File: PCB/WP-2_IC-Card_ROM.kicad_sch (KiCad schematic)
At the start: 9 parts, among them J1 SMS-138-01-G-S, SW1 CUS-12TB, SW2 CUS-12TB, U1 29F0x0_TSOP

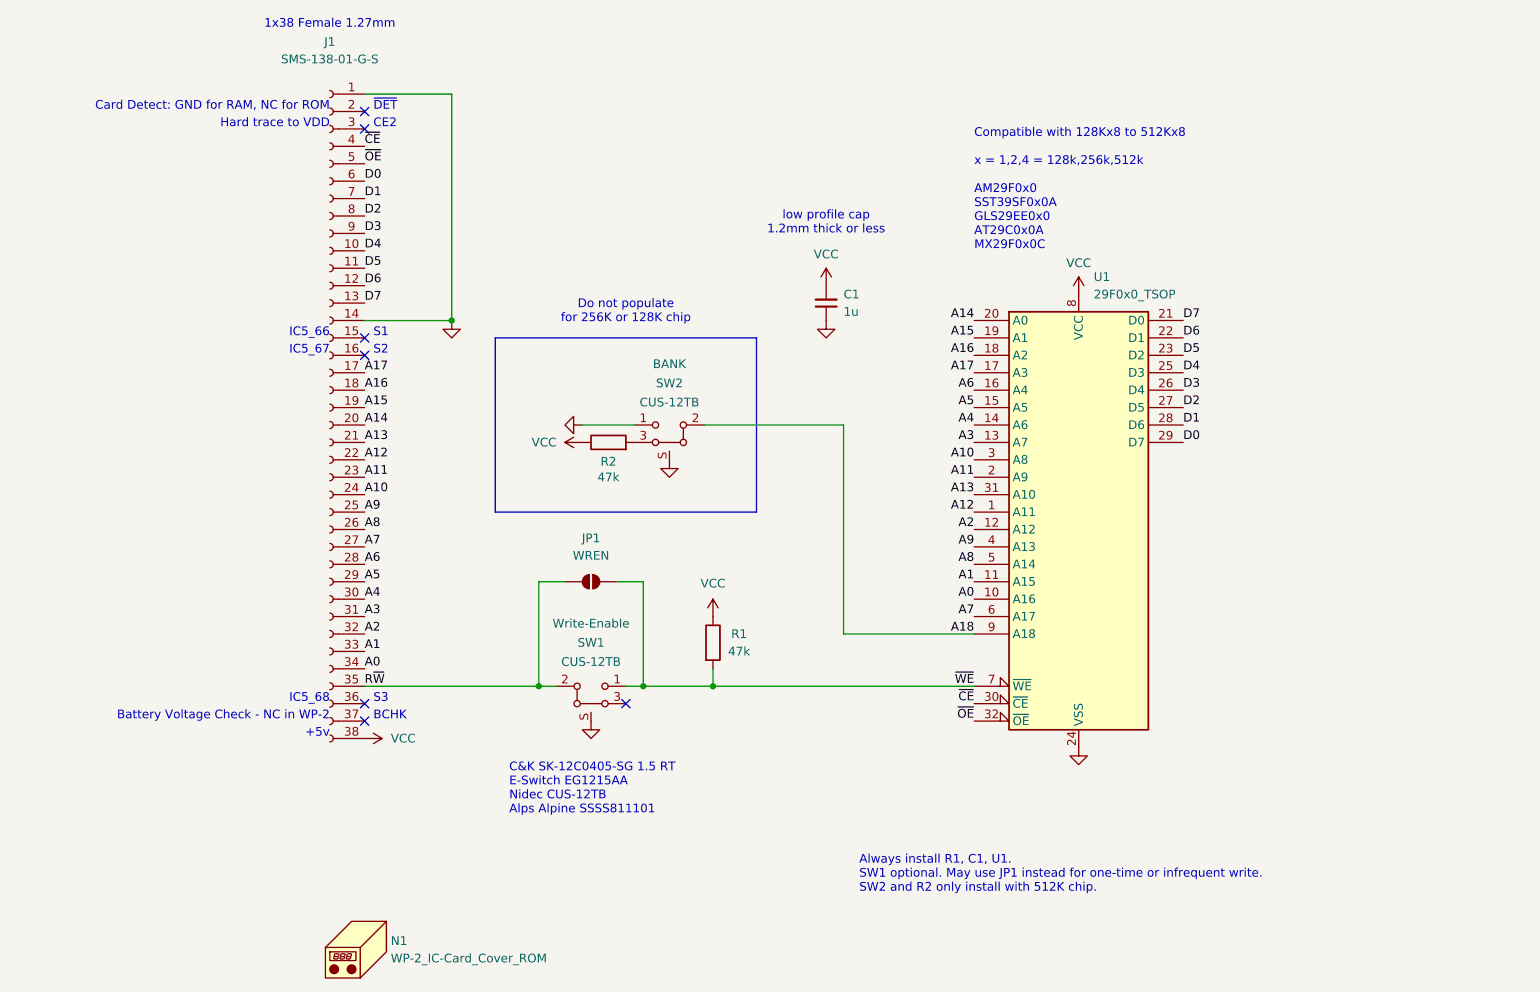
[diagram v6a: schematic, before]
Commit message: SRAM compatible with 512K, pullup /WE, TSOP32 footprint, cfg jumpers
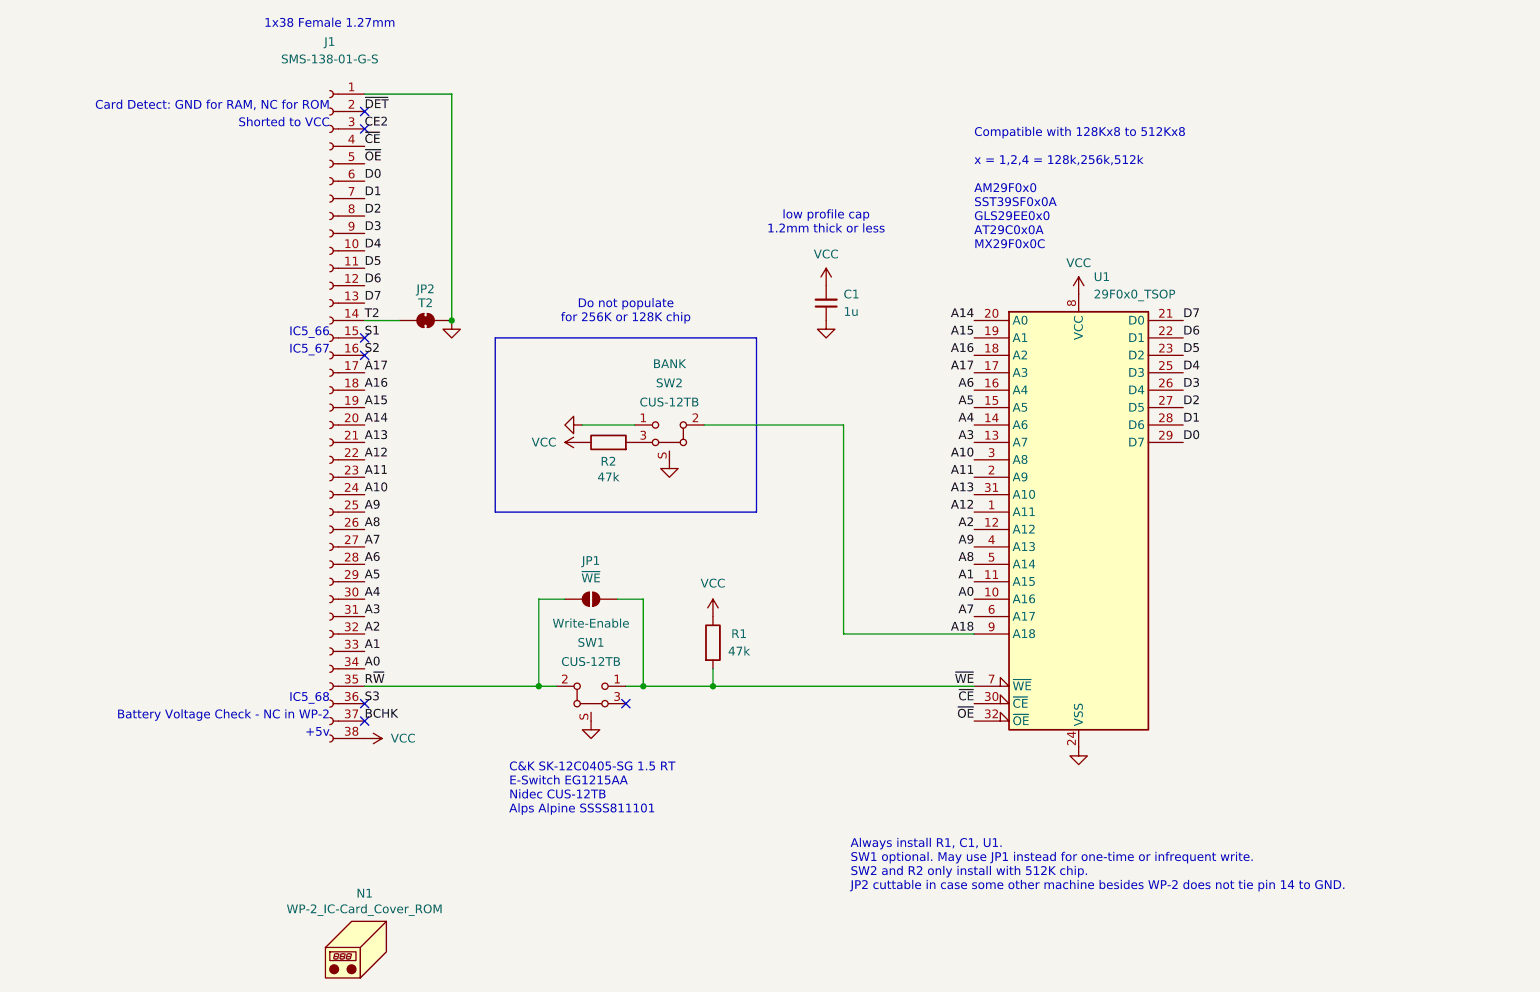
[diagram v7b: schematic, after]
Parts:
- added JP2: T2, 000_LOCAL:SolderJumper-2_P1.3mm_Bridged_RoundedPad1.0x1.5mm, symbol 000_LOCAL:SolderJumper_2_Bridged
- JP1: value WREN -> ~{WE}
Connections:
- net GND: now also JP2.2 (B); no longer J1.14 (Pin_14)
- net S1: now reaches J1.15 (Pin_15)
- net S2: now reaches J1.16 (Pin_16)
- net ~{DET}: now reaches J1.2 (Pin_2)
- net CE2: now reaches J1.3 (Pin_3)
- net S3: now reaches J1.36 (Pin_36)
- net BCHK: now reaches J1.37 (Pin_37)
- new net T2: J1.14 (Pin_14), JP2.1 (A)
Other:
- note added: "Always install R1, C1, U1. SW1 optional. May use JP1 instead for one-time or infrequent write. SW2 and R2 only install with 512K chip. JP2 cuttable in case some other machine besides WP-2 does not tie pin 14 to GND."
- note added: "Shorted to VCC"
- note removed: "Always install R1, C1, U1. SW1 optional. May use JP1 instead for one-time or infrequent write. SW2 and R2 only install with 512K chip."
- note removed: "BCHK"
- note removed: "CE2"
- note removed: "Hard trace to VDD"
- note removed: "S1"
- note removed: "S2"
- note removed: "S3"
- note removed: "~{DET}"
- moved on the sheet: JP1
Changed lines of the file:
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@@
 	(title_block
 		(title "WP-2_IC-Card_ROM")
-		(date "2025-04-20")
-		(rev "008")
+		(date "2025-04-21")
+		(rev "010")
 		(company "Brian K. White - b.kenyon.w@gmail.com")
 		(comment 1 "github.com/bkw777/WP-2_IC-Card")
@@
 	(wire
 		(pts
-			(xy 88.9 86.36) (xy 101.6 86.36)
+			(xy 120.65 101.6) (xy 128.27 101.6)
 		)
 		(stroke
@@
 	(wire
 		(pts
-			(xy 120.65 101.6) (xy 128.27 101.6)
+			(xy 114.3 139.7) (xy 114.3 127)
 		)
 		(stroke
@@
 	(wire
 		(pts
-			(xy 114.3 139.7) (xy 114.3 124.46)
+			(xy 139.7 137.16) (xy 139.7 139.7)
 		)
 		(stroke
@@
 	(wire
 		(pts
-			(xy 139.7 137.16) (xy 139.7 139.7)
+			(xy 129.54 139.7) (xy 139.7 139.7)
 		)
 		(stroke
@@
 	(wire
 		(pts
-			(xy 129.54 139.7) (xy 139.7 139.7)
+			(xy 114.3 127) (xy 118.11 127)
 		)
 		(stroke
@@
 	(wire
 		(pts
-			(xy 114.3 124.46) (xy 118.11 124.46)
+			(xy 101.6 86.36) (xy 101.6 53.34)
 		)
 		(stroke
@@
 	(wire
 		(pts
-			(xy 101.6 86.36) (xy 101.6 53.34)
+			(xy 125.73 127) (xy 129.54 127)
 		)
 		(stroke
@@
 	(wire
 		(pts
-			(xy 125.73 124.46) (xy 129.54 124.46)
+			(xy 127 139.7) (xy 129.54 139.7)
 		)
 		(stroke
@@
 	(wire
 		(pts
-			(xy 127 139.7) (xy 129.54 139.7)
+			(xy 88.9 53.34) (xy 101.6 53.34)
 		)
 		(stroke
@@
 	(wire
 		(pts
-			(xy 88.9 53.34) (xy 101.6 53.34)
+			(xy 88.9 139.7) (xy 114.3 139.7)
 		)
 		(stroke
@@
 	(wire
 		(pts
-			(xy 88.9 139.7) (xy 114.3 139.7)
+			(xy 129.54 127) (xy 129.54 139.7)
 		)
 		(stroke
@@
 	(wire
 		(pts
-			(xy 129.54 124.46) (xy 129.54 139.7)
+			(xy 88.9 86.36) (xy 93.98 86.36)
 		)
 		(stroke
@@
 		)
 	)
-	(text "CE2"
-		(exclude_from_sim no)
-		(at 90.17 58.42 0)
-		(effects
-			(font
-				(size 1.27 1.27)
-			)
-			(justify left bottom)
-		)
-	)
 	(text "+5v"
 		(exclude_from_sim no)
@@
 		)
 	)
-	(text "Always install R1, C1, U1.\nSW1 optional. May use JP1 instead for one-time or infrequent write.\nSW2 and R2 only install with 512K chip.\n"
-		(exclude_from_sim no)
-		(at 161.036 169.926 0)
+	(text "Always install R1, C1, U1.\nSW1 optional. May use JP1 instead for one-time or infrequent write.\nSW2 and R2 only install with 512K chip.\nJP2 cuttable in case some other machine besides WP-2 does not tie pin 14 to GND."
+		(exclude_from_sim no)
+		(at 159.766 169.672 0)
 		(effects
 			(font
@@
 		)
 	)
-	(text "BCHK"
-		(exclude_from_sim no)
-		(at 90.17 144.78 0)
-		(effects
-			(font
-				(size 1.27 1.27)
-			)
-			(justify left bottom)
-		)
-	)
-	(text "~{DET}"
-		(exclude_from_sim no)
-		(at 90.17 55.88 0)
-		(effects
-			(font
-				(size 1.27 1.27)
-			)
-			(justify left bottom)
-		)
-	)
-	(text "S1"
-		(exclude_from_sim no)
-		(at 90.17 88.9 0)
-		(effects
-			(font
-				(size 1.27 1.27)
-			)
-			(justify left bottom)
-		)
-	)
 	(text "1x38 Female 1.27mm"
 		(exclude_from_sim no)
@@
 		)
 	)
-	(text "Hard trace to VDD"
+	(text "Shorted to VCC"
 		(exclude_from_sim no)
 		(at 83.82 58.42 0)
@@
 			)
 			(justify right bottom)
-		)
-	)
-	(text "S2"
-		(exclude_from_sim no)
-		(at 90.17 91.44 0)
-		(effects
-			(font
-				(size 1.27 1.27)
-			)
-			(justify left bottom)
-		)
-	)
-	(text "S3"
-		(exclude_from_sim no)
-		(at 90.17 142.24 0)
-		(effects
-			(font
-				(size 1.27 1.27)
-			)
-			(justify left bottom)
 		)
 	)
@@
 		)
 	)
+	(label "S1"
+		(at 88.9 88.9 0)
+		(fields_autoplaced yes)
+		(effects
+			(font
+				(size 1.27 1.27)
+			)
+			(justify left bottom)
+		)
+	)
 	(label "A6"
 		(at 177.8 96.52 180)
@@
 		)
 	)
+	(label "BCHK"
+		(at 88.9 144.78 0)
+		(fields_autoplaced yes)
+		(effects
+			(font
+				(size 1.27 1.27)
+			)
+			(justify left bottom)
+		)
+	)
 	(label "A13"
 		(at 177.8 111.76 180)
@@
 		)
 	)
+	(label "S2"
+		(at 88.9 91.44 0)
+		(fields_autoplaced yes)
+		(effects
+			(font
+				(size 1.27 1.27)
+			)
+			(justify left bottom)
+		)
+	)
 	(label "D5"
 		(at 88.9 78.74 0)
@@
 		)
 	)
+	(label "S3"
+		(at 88.9 142.24 0)
+		(fields_autoplaced yes)
+		(effects
+			(font
+				(size 1.27 1.27)
+			)
+			(justify left bottom)
+		)
+	)
 	(label "A10"
 		(at 88.9 111.76 0)
@@
 		)
 	)
+	(label "T2"
+		(at 88.9 86.36 0)
+		(fields_autoplaced yes)
+		(effects
+			(font
+				(size 1.27 1.27)
+			)
+			(justify left bottom)
+		)
+	)
 	(label "~{OE}"
 		(at 88.9 63.5 0)
@@
 		)
 	)
+	(label "~{DET}"
+		(at 88.9 55.88 0)
+		(fields_autoplaced yes)
+		(effects
+			(font
+				(size 1.27 1.27)
+			)
+			(justify left bottom)
+		)
+	)
 	(label "A11"
 		(at 177.8 109.22 180)
@@
 			)
 			(justify right bottom)
+		)
+	)
+	(label "CE2"
+		(at 88.9 58.42 0)
+		(fields_autoplaced yes)
+		(effects
+			(font
+				(size 1.27 1.27)
+			)
+			(justify left bottom)
 		)
 	)
@@
 				(path "/f291f000-461a-4127-8876-c8e21ea67ede"
 					(reference "C1")
+					(unit 1)
+				)
+			)
+		)
+	)
+	(symbol
+		(lib_id "000_LOCAL:SolderJumper_2_Bridged")
+		(at 97.79 86.36 0)
+		(unit 1)
+		(exclude_from_sim yes)
+		(in_bom no)
+		(on_board yes)
+		(dnp no)
+		(property "Reference" "JP2"
+			(at 97.79 81.788 0)
+			(effects
+				(font
+					(size 1.27 1.27)
+				)
+			)
+		)
+		(property "Value" "T2"
+			(at 97.79 83.82 0)
+			(effects
+				(font
+					(size 1.27 1.27)
+				)
+			)
+		)
+		(property "Footprint" "000_LOCAL:SolderJumper-2_P1.3mm_Bridged_RoundedPad1.0x1.5mm"
+			(at 97.79 86.36 0)
+			(effects
+				(font
+					(size 1.27 1.27)
+				)
+				(hide yes)
+			)
+		)
+		(property "Datasheet" "~"
+			(at 97.79 86.36 0)
+			(effects
+				(font
+					(size 1.27 1.27)
+				)
+				(hide yes)
+			)
+		)
+		(property "Description" "Solder Jumper, 2-pole, closed/bridged"
+			(at 97.79 86.36 0)
+			(effects
+				(font
+					(size 1.27 1.27)
+				)
+				(hide yes)
+			)
+		)
+		(pin "2"
+		)
+		(pin "1"
+		)
+		(instances
+			(project ""
+				(path "/f291f000-461a-4127-8876-c8e21ea67ede"
+					(reference "JP2")
 					(unit 1)
 				)
@@
 		(on_board yes)
 		(dnp no)
-		(fields_autoplaced yes)
 		(property "Reference" "N1"
-			(at 92.71 176.8474 0)
-			(effects
-				(font
-					(size 1.27 1.27)
-				)
-				(justify left)
+			(at 88.9 169.926 0)
+			(effects
+				(font
+					(size 1.27 1.27)
+				)
 			)
 		)
 		(property "Value" "WP-2_IC-Card_Cover_ROM"
-			(at 92.71 179.3874 0)
-			(effects
-				(font
-					(size 1.27 1.27)
-				)
-				(justify left)
+			(at 88.9 172.212 0)
+			(effects
+				(font
+					(size 1.27 1.27)
+				)
 			)
 		)
@@
 	(symbol
 		(lib_id "000_LOCAL:SolderJumper_2_Open")
-		(at 121.92 124.46 0)
+		(at 121.92 127 0)
 		(unit 1)
 		(exclude_from_sim yes)
@@
 		(on_board yes)
 		(dnp no)
-		(fields_autoplaced yes)
 		(property "Reference" "JP1"
-			(at 121.92 118.11 0)
-			(effects
-				(font
-					(size 1.27 1.27)
-				)
-			)
-		)
-		(property "Value" "WREN"
-			(at 121.92 120.65 0)
+			(at 121.92 121.412 0)
+			(effects
+				(font
+					(size 1.27 1.27)
+				)
+			)
+		)
+		(property "Value" "~{WE}"
+			(at 121.92 123.952 0)
 			(effects
 				(font
@@
 		)
 		(property "Footprint" "000_LOCAL:SolderJumper-2_open"
-			(at 121.92 124.46 0)
+			(at 121.92 127 0)
 			(effects
 				(font
@@
 		)
 		(property "Datasheet" "~"
-			(at 121.92 124.46 0)
+			(at 121.92 127 0)
 			(effects
 				(font
@@
 		)
 		(property "Description" "Solder Jumper, 2-pole, open"
-			(at 121.92 124.46 0)
-			(effects
-				(font
+			(at 121.92 127 0)
+			(effects
+				(font

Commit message: rom solder jumper footprints & pics
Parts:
- JP2: footprint 000_LOCAL:SolderJumper-2_P1.3mm_Bridged_RoundedPad1.0x1.5mm -> 000_LOCAL:SolderJumper-2_Bridged
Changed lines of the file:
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@@
 			)
 		)
-		(property "Footprint" "000_LOCAL:SolderJumper-2_P1.3mm_Bridged_RoundedPad1.0x1.5mm"
+		(property "Footprint" "000_LOCAL:SolderJumper-2_Bridged"
 			(at 97.79 86.36 0)
 			(effects
